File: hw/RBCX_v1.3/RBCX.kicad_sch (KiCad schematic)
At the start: 0 parts

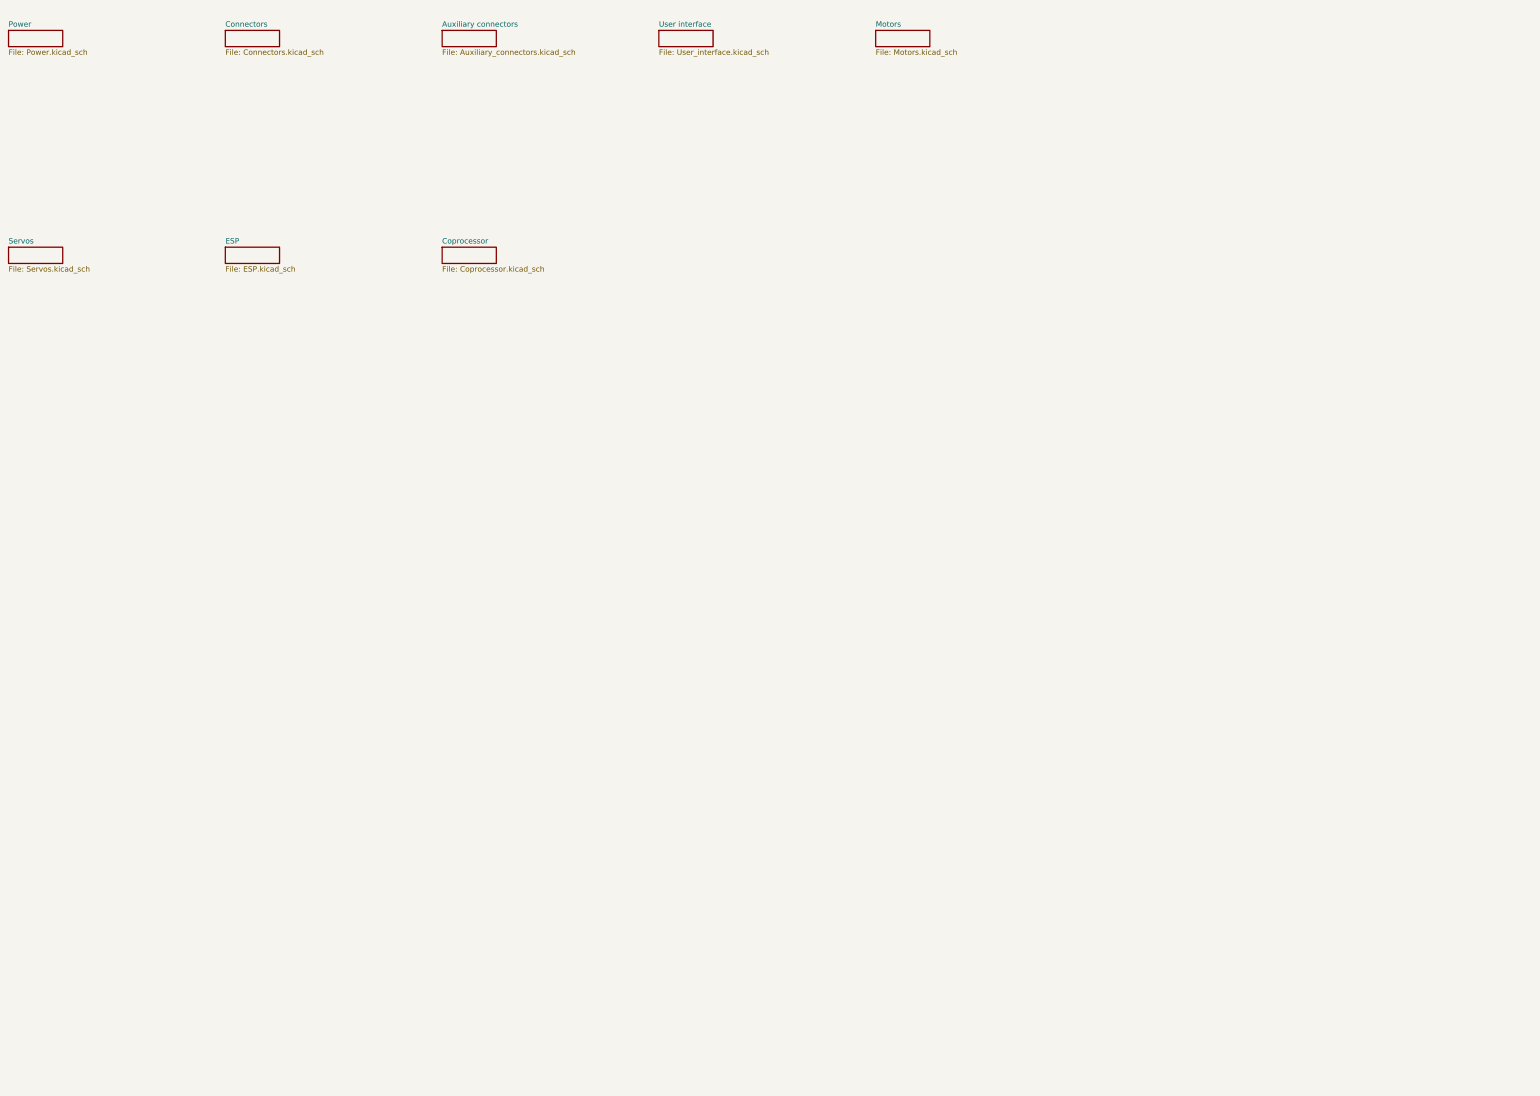
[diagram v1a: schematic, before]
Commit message: Everything everywhere all et once
Conversion to a new look
-  splitting the whole diagram for better orientation on multiple sheets using Kicad functions. Division of the whole schematics within several hierarchical sheets without globally named trac, using only wires, local labels and hierarchical labels.

Add new features
- Battery charger with cell balancer (With whole battery measurement)
- USB PD Sink Controller

Change old features
-  removing many 5V stepdowns and replacing them with only one strong stepdown (continuous 8A, peak 12A)
-  New power switcher design to connect VUSB to the VCC power line when no battery is connected.
(The reason for the new design is the implementation of Power deliveri => high voltage capability on VUSB 5-12V).

Remove micro_USB
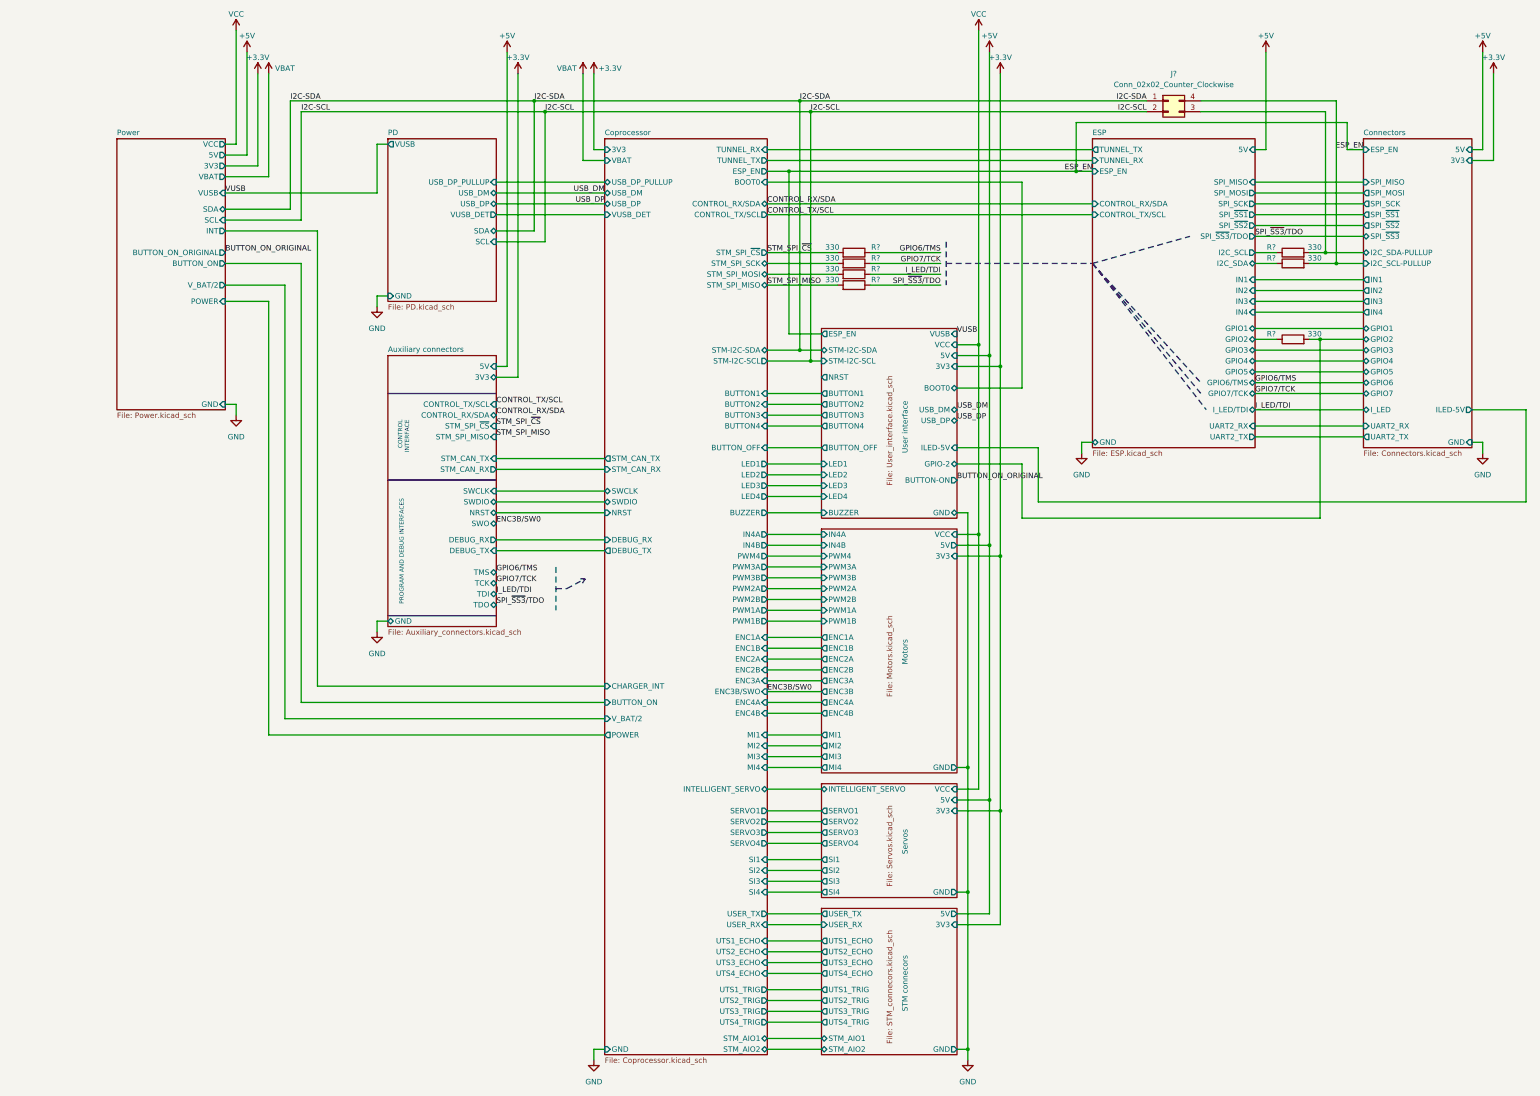
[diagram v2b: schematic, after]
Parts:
- added J?: Conn_02x02_Counter_Clockwise, Connector_PinHeader_2.54mm:PinHeader_2x02_P2.54mm_Vertical, symbol Connector_Generic:Conn_02x02_Counter_Clockwise
- added R? (x7): 330, Capacitor_SMD:C_0201_0603Metric, symbol Device:R
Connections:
- new net Connectors/GPIO2: R?.2
- new net Connectors/I2C_SCL-PULLUP: J?.4 (Pin_4), R?.2
- new net Connectors/I2C_SDA-PULLUP: J?.3 (Pin_3), R?.2
- new net Coprocessor/STM_SPI_MOSI: R?.2
- new net Coprocessor/STM_SPI_SCK: R?.2
- new net ESP/GPIO2: R?.1
- new net ESP/I2C_SCL: R?.1
- new net ESP/I2C_SDA: R?.1
- new net GPIO6/TMS: R?.1
- new net GPIO7/TCK: R?.1
- new net I2C-SCL: J?.2 (Pin_2)
- new net I2C-SDA: J?.1 (Pin_1)
- new net I_LED/TDI: R?.1
- new net SPI_~{SS3}/TDO: R?.1
- new net STM_SPI_MISO: R?.2
- new net STM_SPI_~{CS}: R?.2
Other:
- added sheet PD (PD.kicad_sch)
- added sheet STM connecors (STM_connecors.kicad_sch)
- sheet Auxiliary connectors ports: added 3V3, 5V, CONTROL_RX/SDA, CONTROL_TX/SCL, DEBUG_RX, DEBUG_TX, GND, NRST, STM_CAN_RX, STM_CAN_TX, STM_SPI_MISO, STM_SPI_~{CS}, SWCLK, SWDIO, SWO, TCK, TDI, TDO, TMS; removed none
- sheet Connectors ports: added 3V3, 5V, ESP_EN, GND, GPIO1, GPIO2, GPIO3, GPIO4, GPIO5, GPIO6, GPIO7, I2C_SCL-PULLUP, I2C_SDA-PULLUP, ILED-5V, IN1, IN2, IN3, IN4, I_LED, SPI_MISO, SPI_MOSI, SPI_SCK, SPI_~{SS1}, SPI_~{SS2}, SPI_~{SS3}, UART2_RX, UART2_TX; removed none
- sheet Coprocessor ports: added 3V3, BOOT0, BUTTON1, BUTTON2, BUTTON3, BUTTON4, BUTTON_OFF, BUTTON_ON, BUZZER, CHARGER_INT, CONTROL_RX/SDA, CONTROL_TX/SCL, DEBUG_RX, DEBUG_TX, ENC1A, ENC1B, ENC2A, ENC2B, ENC3A, ENC3B/SWO, ENC4A, ENC4B, ESP_EN, GND, IN4A, IN4B, INTELLIGENT_SERVO, LED1, LED2, LED3, LED4, MI1, MI2, MI3, MI4, NRST, POWER, PWM1A, PWM1B, PWM2A, PWM2B, PWM3A, PWM3B, PWM4, SERVO1, SERVO2, SERVO3, SERVO4, SI1, SI2, SI3, SI4, STM-I2C-SCL, STM-I2C-SDA, STM_AIO1, STM_AIO2, STM_CAN_RX, STM_CAN_TX, STM_SPI_MISO, STM_SPI_MOSI, STM_SPI_SCK, STM_SPI_~{CS}, SWCLK, SWDIO, TUNNEL_RX, TUNNEL_TX, USB_DM, USB_DP, USB_DP_PULLUP, USER_RX, USER_TX, UTS1_ECHO, UTS1_TRIG, UTS2_ECHO, UTS2_TRIG, UTS3_ECHO, UTS3_TRIG, UTS4_ECHO, UTS4_TRIG, VBAT, VUSB_DET, V_BAT/2; removed none
- sheet ESP ports: added 5V, CONTROL_RX/SDA, CONTROL_TX/SCL, ESP_EN, GND, GPIO1, GPIO2, GPIO3, GPIO4, GPIO5, GPIO6/TMS, GPIO7/TCK, I2C_SCL, I2C_SDA, IN1, IN2, IN3, IN4, I_LED/TDI, SPI_MISO, SPI_MOSI, SPI_SCK, SPI_~{SS1}, SPI_~{SS2}, SPI_~{SS3}/TDO, TUNNEL_RX, TUNNEL_TX, UART2_RX, UART2_TX; removed none
- sheet Motors ports: added 3V3, 5V, ENC1A, ENC1B, ENC2A, ENC2B, ENC3A, ENC3B, ENC4A, ENC4B, GND, IN4A, IN4B, MI1, MI2, MI3, MI4, PWM1A, PWM1B, PWM2A, PWM2B, PWM3A, PWM3B, PWM4, VCC; removed none
- sheet Power ports: added 3V3, 5V, BUTTON_ON, BUTTON_ON_ORIGINAL, GND, INT, POWER, SCL, SDA, VBAT, VCC, VUSB, V_BAT/2; removed none
- sheet Servos ports: added 3V3, 5V, GND, INTELLIGENT_SERVO, SERVO1, SERVO2, SERVO3, SERVO4, SI1, SI2, SI3, SI4, VCC; removed none
- sheet User interface ports: added 3V3, 5V, BOOT0, BUTTON-ON, BUTTON1, BUTTON2, BUTTON3, BUTTON4, BUTTON_OFF, BUZZER, ESP_EN, GND, GPIO-2, ILED-5V, LED1, LED2, LED3, LED4, NRST, STM-I2C-SCL, STM-I2C-SDA, USB_DM, USB_DP, VCC, VUSB; removed none
- note added: "CONTROL INTERFACE"
- note added: "PROGRAM AND DEBUG INTERFACES"

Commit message: Work in progress
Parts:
- removed J?: Conn_02x02_Counter_Clockwise, Connector_PinHeader_2.54mm:PinHeader_2x02_P2.54mm_Vertical, symbol Connector_Generic:Conn_02x02_Counter_Clockwise
- added J1: Conn_02x02_Odd_Even, Connector_PinHeader_2.54mm:PinHeader_2x02_P2.54mm_Vertical, symbol Connector_Generic:Conn_02x02_Odd_Even
- added JP? (x2): SolderJumper_2_Bridged, Jumper:SolderJumper-2_P1.3mm_Bridged_RoundedPad1.0x1.5mm, symbol Jumper:SolderJumper_2_Bridged
- gave numbers to parts that had none: 7
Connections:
- net Connectors/I2C_SCL-PULLUP: now also R2.2, J1.3 (Pin_3); no longer R4.2
- net Connectors/I2C_SDA-PULLUP: now also R4.2, J1.1 (Pin_1); no longer R2.2
- net I2C-SCL: now also J1.4 (Pin_4)
- net I2C-SDA: now also J1.2 (Pin_2)
- net USB_DM: now also JP?.1 (A)
- net USB_DP: now also JP?.1 (A)
- new net STM_AIO1: JP?.2 (B)
- new net STM_AIO2: JP?.2 (B)
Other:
- note added: "DAC PIN TO USB CONNECTION TO SUPPORT QUICK CHARGING"
- moved on the sheet: R2, R4

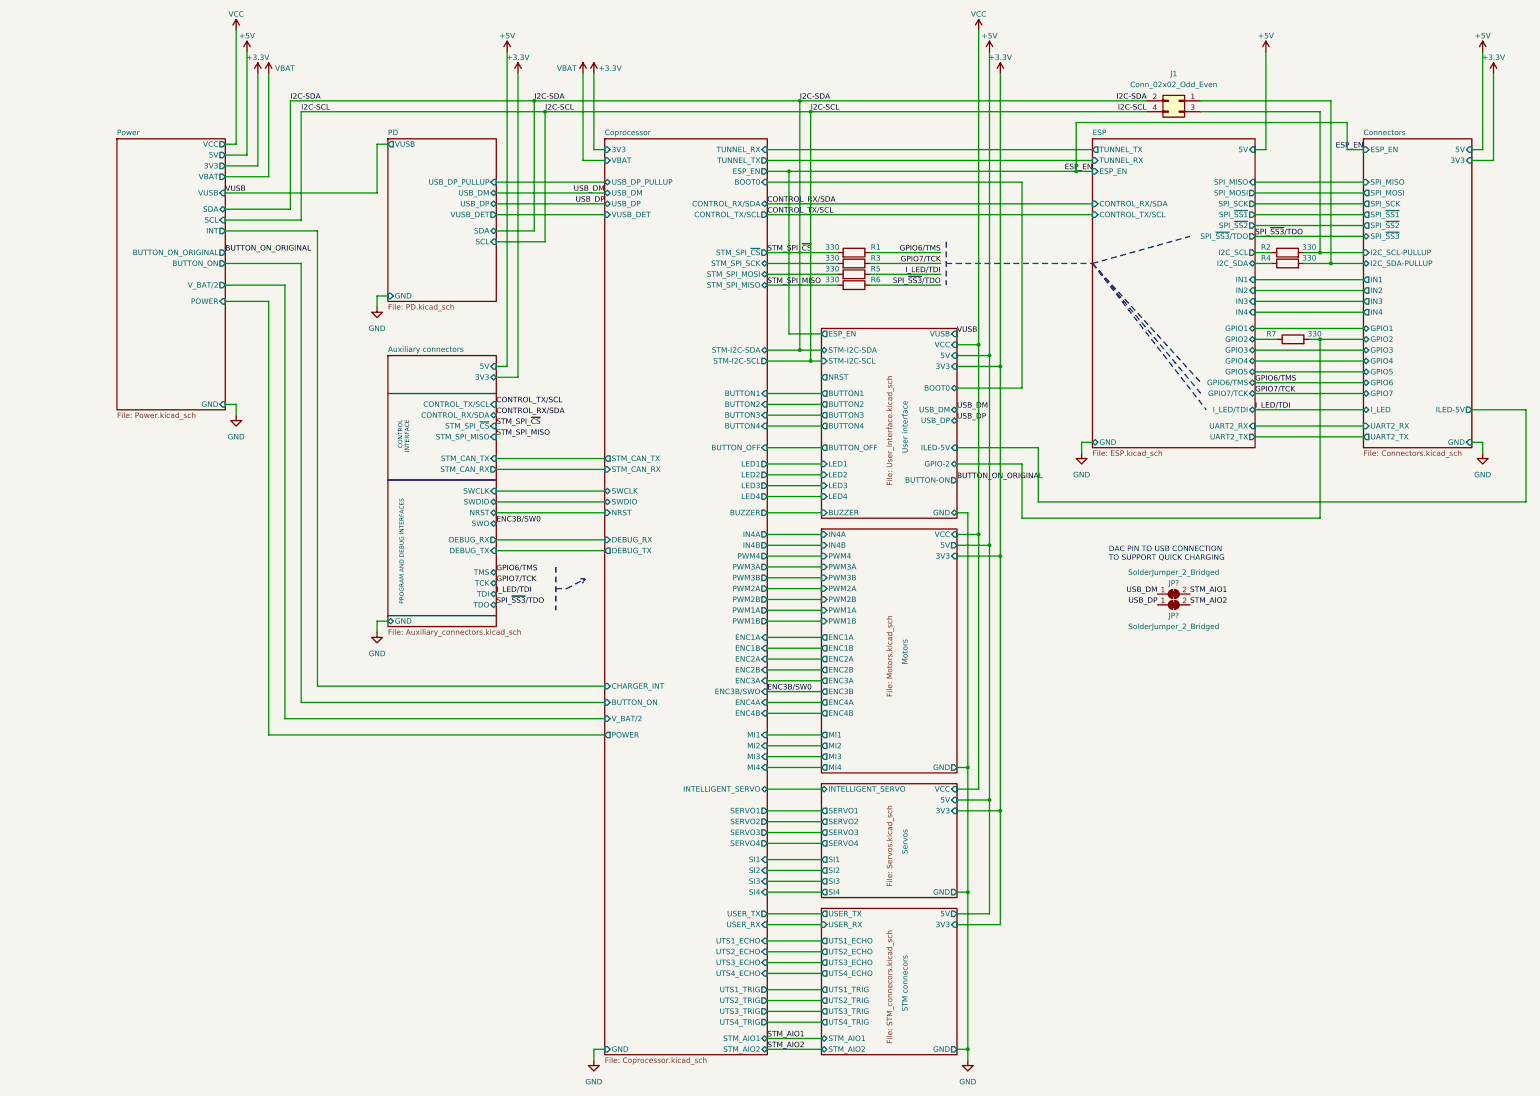
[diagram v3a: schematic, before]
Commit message: New PCB layout
some changes of schema:
- change PD sink AO33772 to AO33771
- remove power switch
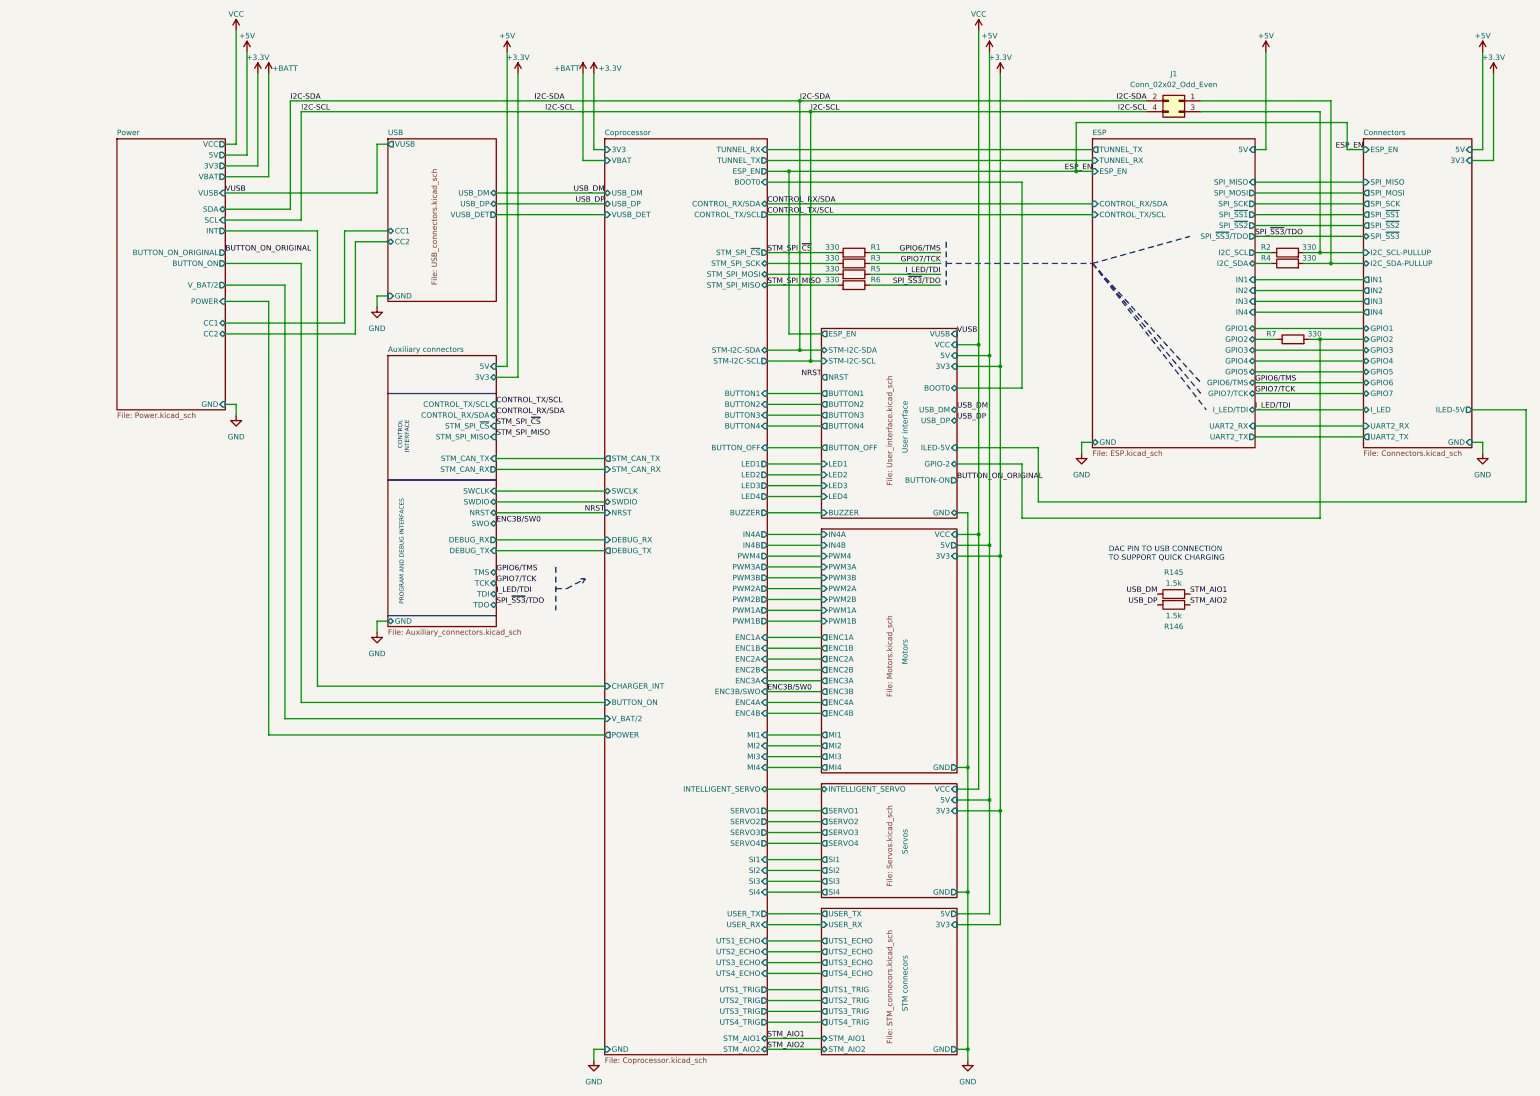
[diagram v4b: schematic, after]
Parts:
- removed JP? (x2): SolderJumper_2_Bridged, Jumper:SolderJumper-2_P1.3mm_Bridged_RoundedPad1.0x1.5mm, symbol Jumper:SolderJumper_2_Bridged
- added R145, R146: 1.5k, Resistor_SMD:R_0402_1005Metric, symbol Device:R
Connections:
- net STM_AIO1: now also R145.2
- net STM_AIO2: now also R146.1
- net USB_DM: now also R145.1
- net USB_DP: now also R146.2
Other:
- sheet PD renamed USB
- sheet Coprocessor ports: added none; removed USB_DP_PULLUP
- sheet Power ports: added CC1, CC2; removed none
- sheet USB: file PD.kicad_sch -> USB_connectors.kicad_sch
- sheet USB ports: added CC1, CC2; removed SCL, SDA, USB_DP_PULLUP

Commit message: Production files
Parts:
- J1: JLCPCB_CORRECTION (none) -> 1.27;1.27;0
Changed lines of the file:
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@@
+      (effects (font (size 1.27 1.27)) hide)
+    )
+    (property "JLCPCB_CORRECTION" "1.27;1.27;0" (id 6) (at 299.72 41.91 0)
       (effects (font (size 1.27 1.27)) hide)
     )

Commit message: correction of USP-C footprint
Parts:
- J1: JLCPCB_CORRECTION 1.27;1.27;0 -> 1.27;-1.27;-90
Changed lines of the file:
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@@
       (effects (font (size 1.27 1.27)) hide)
     )
-    (property "JLCPCB_CORRECTION" "1.27;1.27;0" (id 6) (at 299.72 41.91 0)
+    (property "JLCPCB_CORRECTION" "1.27;-1.27;-90" (id 6) (at 299.72 41.91 0)
       (effects (font (size 1.27 1.27)) hide)
     )
